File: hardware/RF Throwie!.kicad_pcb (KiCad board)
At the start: 2 copper layers, 20.9 x 20.7 mm, 28 parts, among them J1 Conn_01x04, J2 Conn_Coaxial, J4 PROG, U1 CH32V003FxUx, U2 CMT2119A, U3 ME6118, Y2 26MHz

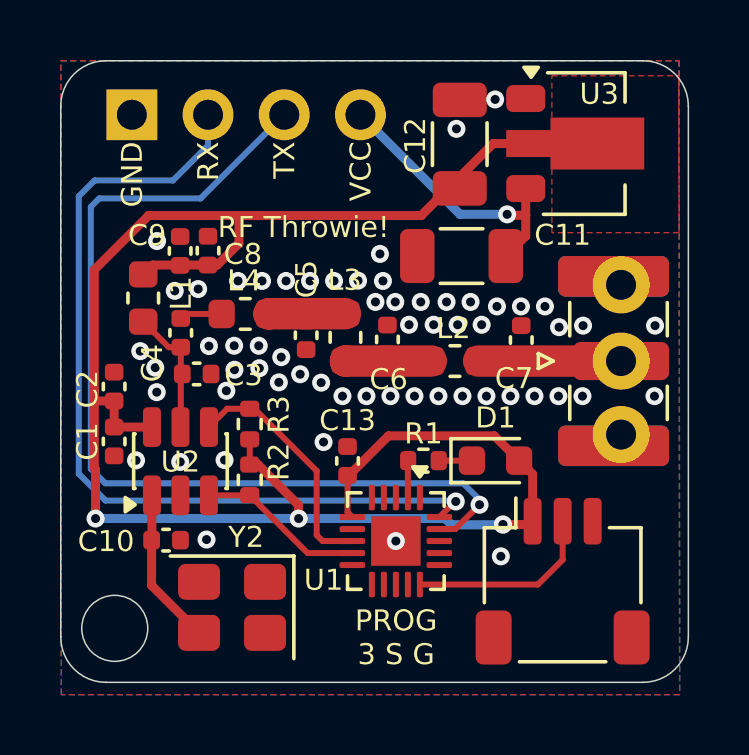
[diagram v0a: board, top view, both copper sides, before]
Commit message: Add RX->DATA and TX->CLK jumpers, add more helpful silkscreen, fix SMA connector footprint
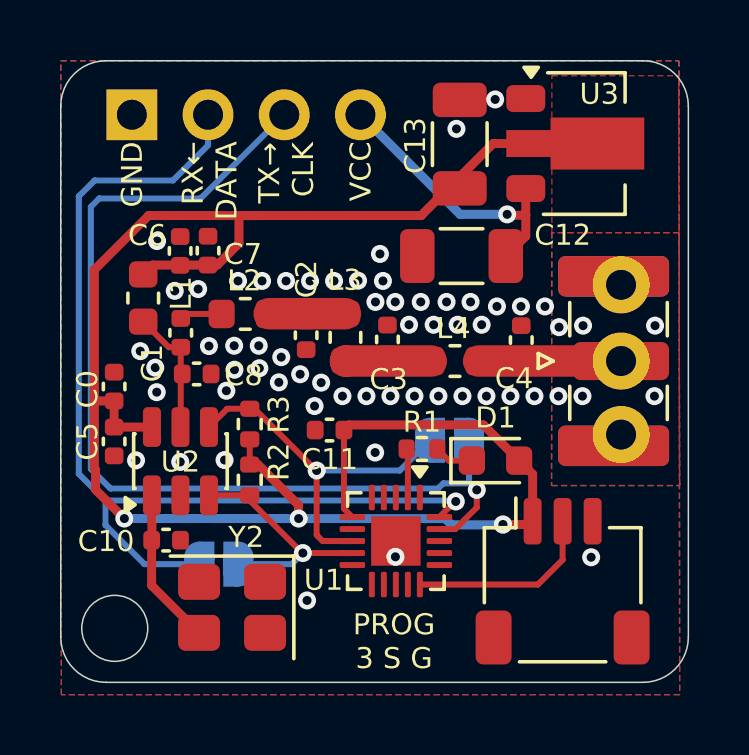
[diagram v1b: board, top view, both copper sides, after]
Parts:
- added JP1: SolderJumper_2_Open, Jumper:SolderJumper-2_P1.3mm_Open_RoundedPad1.0x1.5mm, B.Cu at (132.3, 98.9)
- added JP2: SolderJumper_2_Open, Jumper:SolderJumper-2_P1.3mm_Open_RoundedPad1.0x1.5mm, B.Cu at (140.0, 94.8)
- C10: value C -> DNP
- C2: renamed from C5; value 18p -> 10p
- C3: renamed from C6; value 27p -> 5.1p
- C4: renamed from C7; value 9p -> DNP
- C7: renamed from C8; value 220p -> DNP
- C8: renamed from C3; value C -> TBD
- J1: value Conn_01x04 -> PWR+UART
- L1: value 180n -> 100n
- L2: renamed from L4; value 62n -> 5.6n
- L3: value 27n -> 8.2n
- L4: renamed from L2; value 27n -> short
- U3: value ME6118 -> ME6118A33PG
- moved C11 1.19 mm to (136.0, 94.5), turned to 180 degrees
- moved R1 0.39 mm to (139.1, 95.1)
- renumbered C2 to C0, C4 to C1, C13 to C11, C11 to C12, C12 to C13, C1 to C5, C9 to C6
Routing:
- net RX: track 29.0 -> 33.5 mm
- net CLK: track 8.11 -> 12.3 mm, vias 0 -> 1
- net DATA: track 5.57 -> 7.98 mm, vias 0 -> 1
- net TX: track 31.7 -> 33.6 mm
- net +3.3V: track 60.9 -> 61.7 mm
- net GND: vias 60 -> 61
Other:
- board text added: "RF Throwie! v1.3"
- board text added: "RX->DATA"
- board text added: "RX← DATA"
- board text added: "TX->CLK"
- board text added: "TX→ CLK"
- board text added: "←TX CLK"
- board text added: "→RX DATA"
- board text removed: "RF Throwie!"
- board text removed: "RF Throwie! v1.2"
- board text removed: "RX"
- board text removed: "TX"
